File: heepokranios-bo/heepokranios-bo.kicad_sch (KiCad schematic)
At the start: 122 parts, among them J1 Conn_02x02_Odd_Even, J11 PGA_13x13, J12 Conn_01x08_Pin, J13 Conn_01x08_Socket, J2 Conn_02x02_Odd_Even, J20 Conn_01x05, J21 Conn_01x03, J22 Conn_01x03, J3 Conn_02x03_Odd_Even, J4 Conn_02x03_Odd_Even, J5 Conn_02x03_Odd_Even, J6 Conn_02x04_Odd_Even, J8 Conn_02x03_Odd_Even, J9 Conn_02x02_Odd_Even, SW1 SW_Push

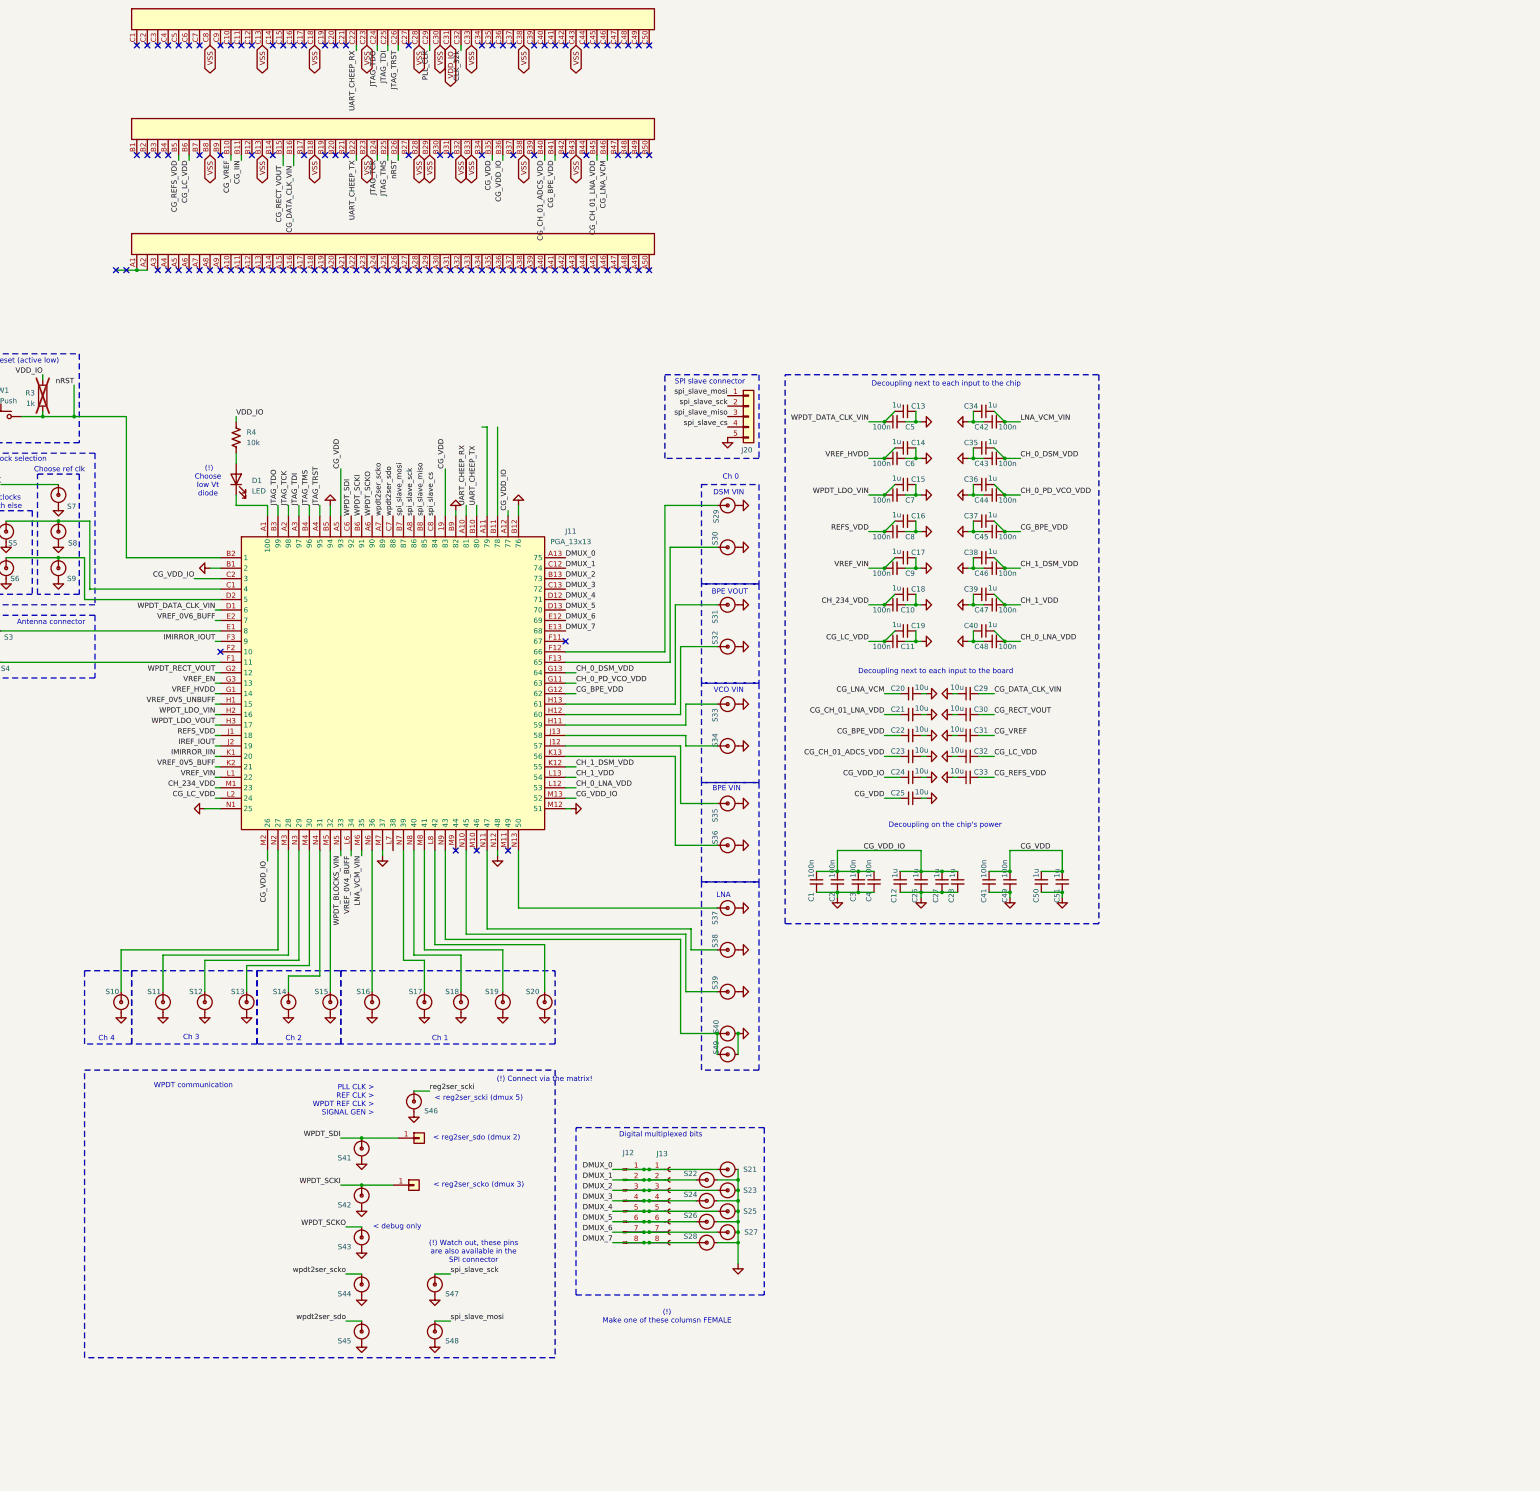
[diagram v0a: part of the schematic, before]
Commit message: Added GPIO playground extension board
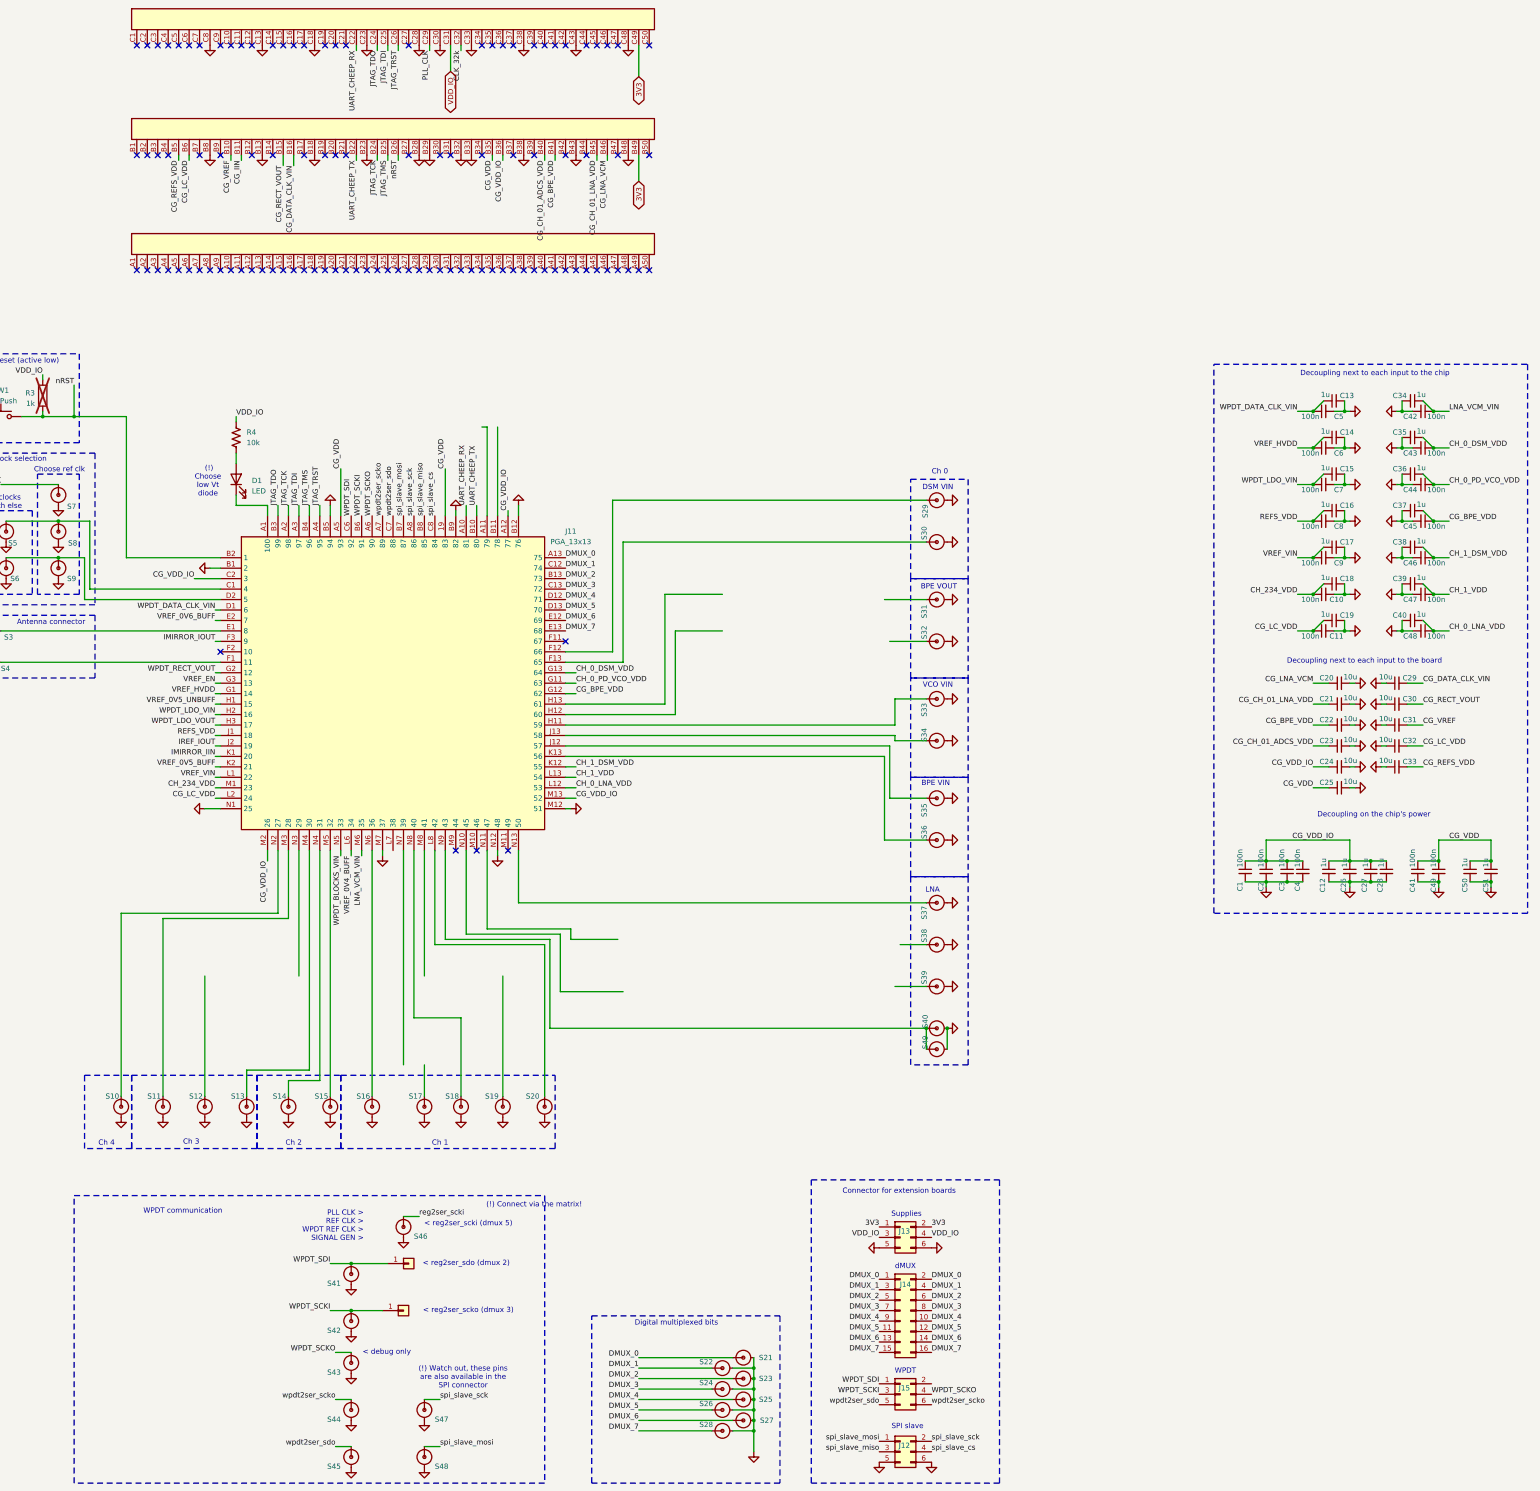
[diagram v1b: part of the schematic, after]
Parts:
- removed J12: Conn_01x08_Pin, Connector_PinHeader_2.54mm:PinHeader_1x08_P2.54mm_Vertical, symbol Connector:Conn_01x08_Pin
- removed J13: Conn_01x08_Socket, Connector_PinHeader_2.54mm:PinHeader_1x08_P2.54mm_Vertical, symbol Connector:Conn_01x08_Socket
- removed J20: Conn_01x05, Connector_PinHeader_2.54mm:PinHeader_1x05_P2.54mm_Vertical, symbol Connector_Generic:Conn_01x05
- added J12, J13, J15: Conn_02x03_Odd_Even, Connector_PinSocket_2.54mm:PinSocket_2x03_P2.54mm_Horizontal, symbol Connector_Generic:Conn_02x03_Odd_Even
- added J14: Conn_02x08_Odd_Even, Connector_PinSocket_2.54mm:PinSocket_2x08_P2.54mm_Horizontal, symbol Connector_Generic:Conn_02x08_Odd_Even
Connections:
- net VSS is gone; now on net GND: J10.B13, J10.B18, J10.B23, J10.B28, J10.B29, J10.B32, J10.B33, J10.B38, J10.B43, J10.B8, J10.C13, J10.C18, J10.C23, J10.C28, J10.C30, J10.C33, J10.C38, J10.C43, J10.C8
- net DMUX_0: now also J14.1 (Pin_1), J14.2 (Pin_2)
- net DMUX_1: now also J14.3 (Pin_3), J14.4 (Pin_4)
- net DMUX_2: now also J14.5 (Pin_5), J14.6 (Pin_6)
- net DMUX_3: now also J14.7 (Pin_7), J14.8 (Pin_8)
- net DMUX_4: now also J14.10 (Pin_10), J14.9 (Pin_9)
- net DMUX_5: now also J14.11 (Pin_11), J14.12 (Pin_12)
- net DMUX_6: now also J14.13 (Pin_13), J14.14 (Pin_14)
- net DMUX_7: now also J14.15 (Pin_15), J14.16 (Pin_16)
- net GND: now also J10.B48, J10.C48, J12.5 (Pin_5), J12.6 (Pin_6), J13.5 (Pin_5), J13.6 (Pin_6)
- net VDD_IO: now also J13.3 (Pin_3), J13.4 (Pin_4)
- net WPDT_SCKI: now also J15.3 (Pin_3)
- net WPDT_SCKO: now also J15.4 (Pin_4)
- net WPDT_SDI: now also J15.1 (Pin_1)
- net spi_slave_cs: now also J12.4 (Pin_4)
- net spi_slave_miso: now also J12.3 (Pin_3)
- net spi_slave_mosi: now also J12.1 (Pin_1)
- net spi_slave_sck: now also J12.2 (Pin_2)
- net wpdt2ser_scko: now also J15.6 (Pin_6)
- net wpdt2ser_sdo: now also J15.5 (Pin_5)
- net at S38.1: no longer J11.N11 (47)
- net at S19.1: no longer J11.M8 (41)
- net at S31.1: no longer J11.H13 (61)
- net at S32.1: no longer J11.H12 (60)
- net at S17.1: no longer J11.N7 (39)
- net at S12.1: no longer J11.N3 (29)
- net at J11.N10 (45): no longer S39.1
- net at J10.A1: no longer J10.A2
- net 3V3: now reaches J10.B49
- net 3V3: now also J10.C49, J13.1 (Pin_1), J13.2 (Pin_2)
- no-connect marks 113 -> 109
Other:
- note added: "Connector for extension boards"
- note added: "SPI slave"
- note added: "Supplies"
- note added: "WPDT"
- note added: "dMUX"
- note removed: "(!) Make one of these columsn FEMALE"
- note removed: "SPI slave connector"
- moved on the sheet: C1, C10, C11, C12, C13, C14, C15, C16, C17, C18, C19, C2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

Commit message: Added floorplan and outline of breakout board
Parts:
- removed J21, J22: Conn_01x03, Connector_PinHeader_2.54mm:PinHeader_1x01_P2.54mm_Vertical, symbol Connector_Generic:Conn_01x01
- removed S46: SMA connector, heepokranios-bo-library:SMA_w_tp, symbol heepokranios-bo-library:SMA_w_tp
- added C73: 100n, Capacitor_SMD:C_0603_1608Metric, symbol Device:C_Small
- added C74: 1u, Capacitor_SMD:C_0603_1608Metric, symbol Device:C_Small
- J10, J7: value ~ -> (none)
- J11: footprint PGA_socket:PGA_13x13 -> PGA13x13
- renumbered J13 to J14, J14 to J15, J15 to J16, J12 to J17, S41 to S16, S42 to S17, S43 to S18, S44 to S19, S45 to S20, S16 to S21, S17 to S23, S47 to S24, S48 to S25, S18 to S26, S19 to S27, S20 to S28, S22 to S29, S24 to S30, S26 to S31, S28 to S32, S21 to S33, S23 to S34, S25 to S35, S27 to S36, S29 to S37, S30 to S38, S31 to S39, S32 to S40, S33 to S41, S34 to S42, S35 to S43, S36 to S44, S37 to S45, S38 to S46, S39 to S47, S40 to S48
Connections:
- net CG_VDD: now also J11.A9 (83); no longer J11.19 (83)
- net GND: now also C73.2, C74.2
- net WPDT_BLOCKS_VIN: now also C73.1, C74.1
- net Buffer_0/OUT_P: now reaches S46.1
- net Buffer_2/OUT_P: now reaches S27.1
- net Buffer_1/OUT_P: now reaches S39.1
- net Buffer_1/OUT_N: now reaches S40.1
- net Buffer_2/OUT_N: now reaches S23.1
- net SE_buffer_2/VOUT: now reaches S12.1
- net Buffer_1/VIN_N: now reaches J11.H12 (60)
- net Buffer_1/VIN_P: now reaches J11.H13 (61)
- net Buffer_2/VIN_P: now reaches J11.M8 (41)
- net Buffer_0/VIN_N: now reaches J11.N10 (45)
- net Buffer_0/VIN_P: now reaches J11.N11 (47)
- net SE_buffer_2/VIN: now reaches J11.N3 (29)
- net Buffer_2/VIN_N: now reaches J11.N7 (39)
- net Buffer_0/OUT_N: now reaches S47.1
- no-connect marks 109 -> 111
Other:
- added sheet Buffer_0 (subsheets/fd_buffer.kicad_sch)
- added sheet Buffer_1 (subsheets/fd_buffer.kicad_sch)
- added sheet Buffer_2 (subsheets/fd_buffer.kicad_sch)
- added sheet SE_buffer_2 (subsheets/se_buffer.kicad_sch)
- note added: "(!) Add test points before buffer"
- note added: "(!) Connect to tri-state switches!"
- note added: "(!) Nati revise"
- note added: "(!) VREF_EN add pull-down. This one is 1.2 V"
- note added: "Power and reference for the external buffers"
- note added: "VCM of the LNA and WPDT blocks"
- note added: "VDD for the channel's ADCs"
- note added: "VDD for the channel's LNAs"
- note removed: "(!) Connect via the matrix!"
- note removed: "Reference for the channel's ADCs"
- note removed: "Reference for the channel's LNAs"
- note removed: "VCM/WPDT blocks"
- moved on the sheet: C1, C10, C11, C12, C13, C14, C15, C16, C17, C18, C19, C2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
